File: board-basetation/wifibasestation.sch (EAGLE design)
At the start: 33 parts, among them IC1 1117EMP, IC2 STM32F072, IC3 HTU21D, J1 SWD_SHROUD_SMD, X1 ESP-03, X2 SMA-142-0711-821/826

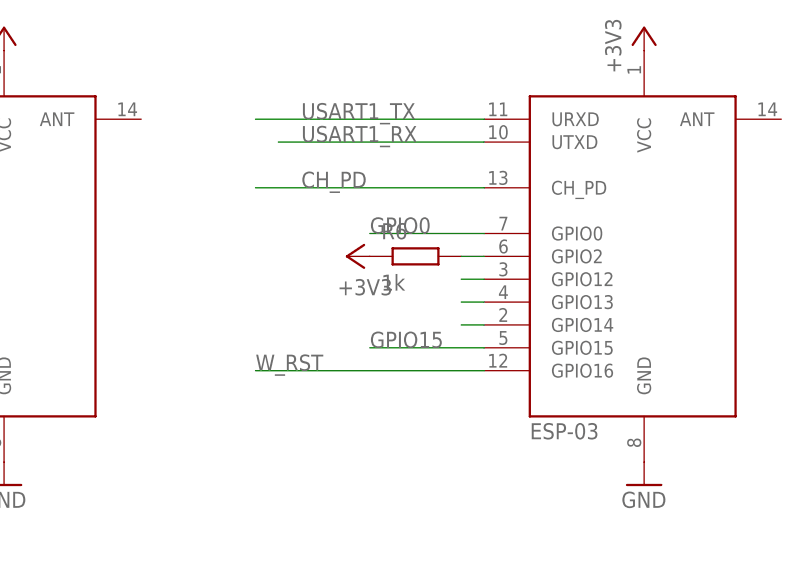
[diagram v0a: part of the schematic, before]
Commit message: adding stencil and couple of values
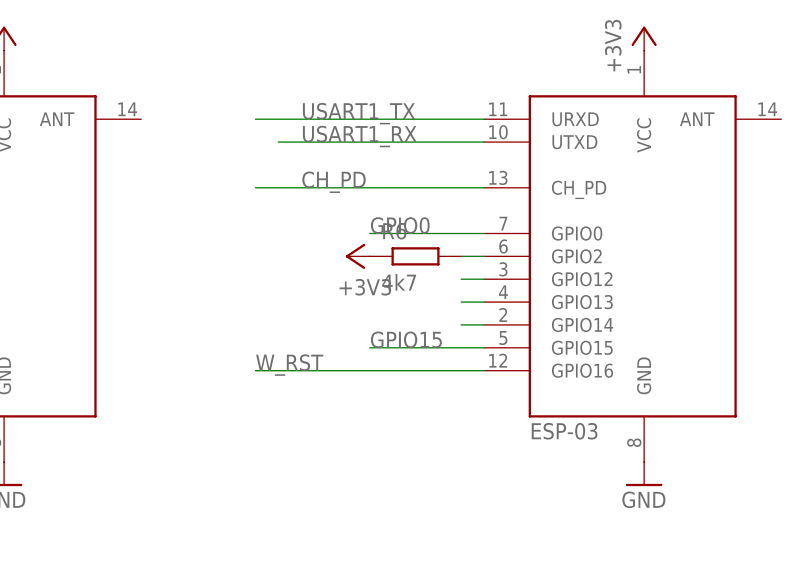
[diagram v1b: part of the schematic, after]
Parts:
- R6: value 1k -> 4k7
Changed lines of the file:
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@@
 <part name="GND22" library="supply1" deviceset="GND" device=""/>
 <part name="+3V14" library="supply1" deviceset="+3V3" device=""/>
-<part name="R6" library="passives-7351" deviceset="RESISTOR" device="0603-N" value="1k"/>
+<part name="R6" library="passives-7351" deviceset="RESISTOR" device="0603-N" value="4k7"/>
 <part name="+3V15" library="supply1" deviceset="+3V3" device=""/>
 <part name="U$3" library="Mine" deviceset="ESP-07" device=""/>

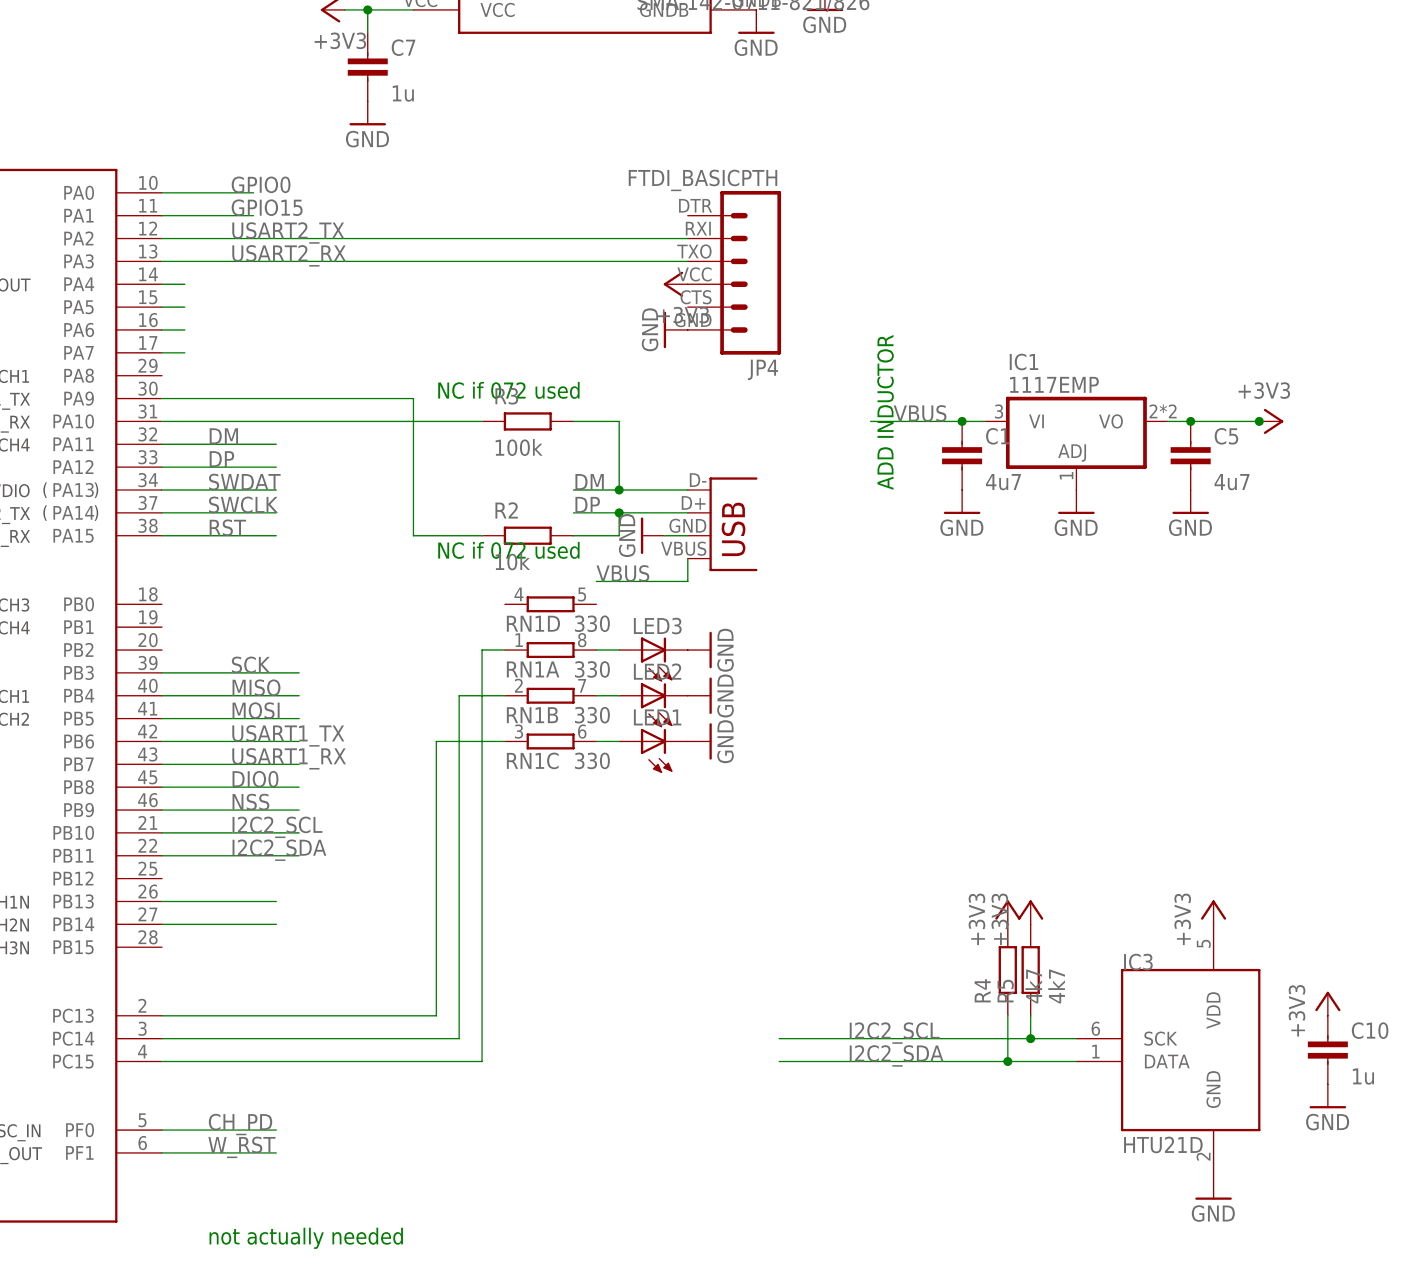
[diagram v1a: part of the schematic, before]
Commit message: HARDWARE: removes FTDI, HTU21
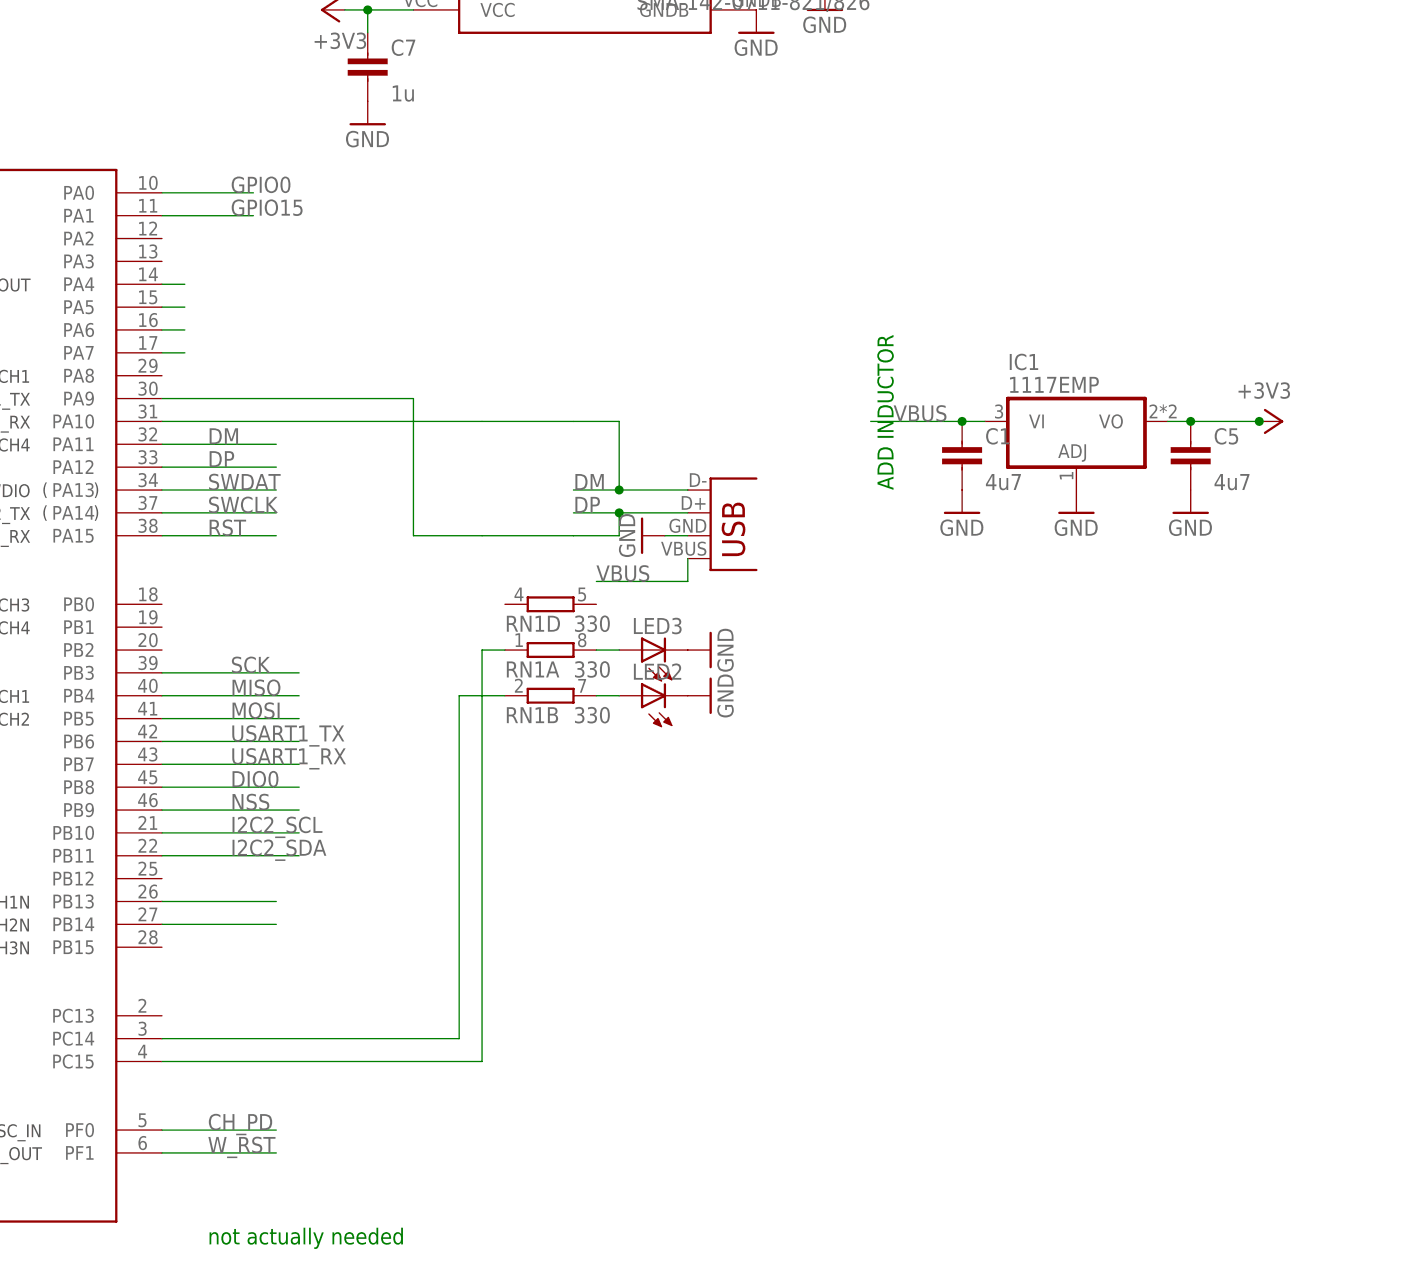
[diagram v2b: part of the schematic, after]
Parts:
- removed C10: 1u, passives-7351:CAPACITOR0603-N
- removed IC3: HTU21D, Mine:HTU21D
- removed JP4: FTDI_BASICPTH, SparkFun-Connectors:FTDI_BASICPTH
- removed LED1: (no value), led:LEDCHIP-LED0805
- removed R2: 10k, passives-7351:RESISTOR0603-N
- removed R3: 100k, passives-7351:RESISTOR0603-N
- removed R4, R5: 4k7, passives-7351:RESISTOR0603-N
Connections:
- removed net N$17: IC2.PA10, R3.P$1
- removed net N$18: IC2.PA9, R2.P$1
- removed net N$2: IC2.PC13, RN1C.1
- removed net N$20: LED1.A, RN1C.2
- removed net USART2_RX: IC2.PA3, JP4.3
- removed net USART2_TX: IC2.PA2, JP4.2
- net +3V3: no longer C10.1, IC3.VDD, JP4.4, R4.P$2, R5.P$2
- net DM: now also IC2.PA10; no longer R3.P$2
- net DP: now also IC2.PA9; no longer R2.P$2
- net GND: no longer C10.2, IC3.GND, JP4.6, LED1.C
- net I2C2_SCL: no longer IC3.SCK, R5.P$1
- net I2C2_SDA: no longer IC3.DATA, R4.P$1
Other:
- note removed: "NC if 072 used"

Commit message: HARDWARE: switch to ESP12
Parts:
- removed LED2: (no value), led:LEDCHIP-LED0805
- removed R6: 4k7, passives-7351:RESISTOR0603-N
- removed RN1: 330, resistor-dil:4R-NEXB38V
- removed S1: SWITCH-MOMENTARY-2SMD-1101NE, SparkFun-Electromechanical:SWITCH-MOMENTARY-2SMD-1101NE
- removed U$3: ESP-07, Mine:ESP-07
- removed X1: ESP-03, Mine:ESP-03
- added R2, R3: (no value), passives-7351:RESISTOR0603-N
- added TP1, TP2: TEST-POINT2, SparkFun-Connectors:TEST-POINT2
- added U$1: ESP8266_ESP-12, ESP8266-ESP12:ESP8266_ESP-12
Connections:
- removed net N$10: LED2.A, RN1B.2
- removed net N$21: IC2.PC14, RN1B.1
- removed net N$3: U$3.GPIO14, X1.GPIO14
- removed net N$4: U$3.GPIO13, X1.GPIO13
- removed net N$7: U$3.GPIO12, X1.GPIO12
- new net N$20: U$1.REST
- net +3V3: now also R2.P$2, TP1.1, U$1.VCC; no longer R6.P$1, S1.2, U$3.VCC, X1.VCC
- net CH_PD: now also U$1.CH_PD; no longer U$3.CH_PD, X1.CH_PD
- net GND: now also U$1.GND; no longer LED2.C, U$3.GND, X1.GND
- net GPIO0: no longer U$3.GPIO0, X1.GPIO0
- net GPIO15: now also U$1.GPIO15; no longer U$3.GPIO15, X1.GPIO15
- net N$1: now also R2.P$1, U$1.GPIO2; no longer R6.P$2, U$3.GPIO2, X1.GPIO2
- net N$15: now also TP2.1; no longer S1.1
- net N$22: now also R3.P$1; no longer RN1A.1
- net N$9: now also R3.P$2; no longer RN1A.2
- net USART1_RX: now also U$1.TXD; no longer U$3.UTXD, X1.UTXD
- net USART1_TX: now also U$1.RXD; no longer U$3.URXD, X1.URXD
- net W_RST: no longer U$3.GPIO16, X1.GPIO16
